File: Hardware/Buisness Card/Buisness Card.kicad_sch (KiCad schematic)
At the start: 24 parts, among them J101 USB_A, J102 Conn_01x03_Male, J103 Tag Connect, U101 NCP1117-12_SOT223, U102 ATtiny85-20S, U103 ProtoBoard

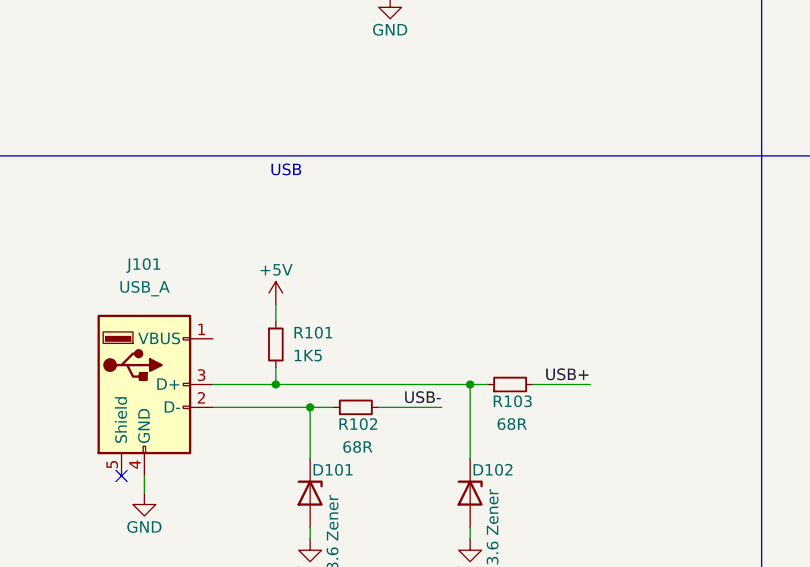
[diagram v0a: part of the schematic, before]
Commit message: put diode in the right way
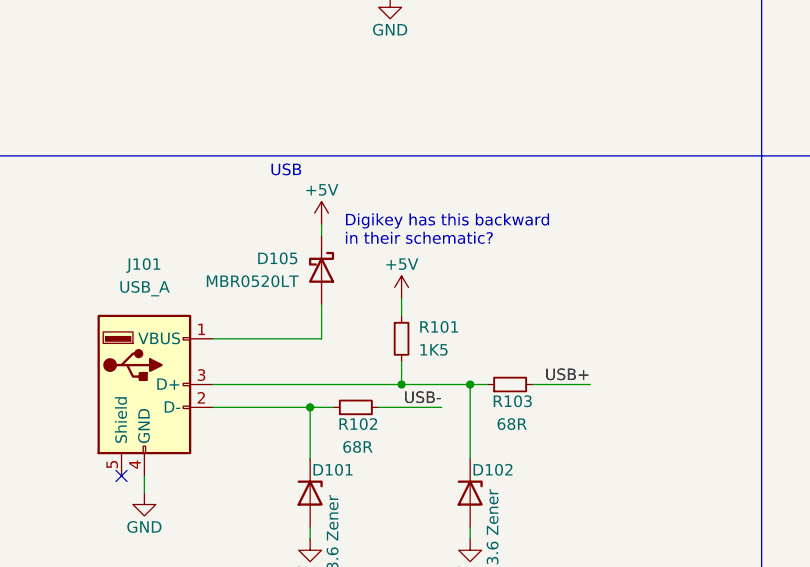
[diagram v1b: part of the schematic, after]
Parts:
- added D105: MBR0520LT, Diode_SMD:D_SOD-123, symbol Diode:MBR0520LT
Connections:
- net +5V: now also D105.1 (K)
- net at J101.1 (VBUS): now also D105.2 (A)
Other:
- note added: "Digikey has this backward in their schematic?"
- moved on the sheet: R101
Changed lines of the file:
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@@
   (junction (at 81.915 35.56) (diameter 0) (color 0 0 0 0)
   )
-  (junction (at 57.15 91.44) (diameter 0) (color 0 0 0 0)
+  (junction (at 71.12 91.44) (diameter 0) (color 0 0 0 0)
   )
   (junction (at 78.74 91.44) (diameter 0) (color 0 0 0 0)
@@
     (stroke (width 0) (type default) (color 0 0 0 0))
   )
-  (wire (pts (xy 57.15 91.44) (xy 57.15 89.535))
-    (stroke (width 0) (type default) (color 0 0 0 0))
-  )
   (wire (pts (xy 137.795 185.42) (xy 150.495 185.42))
     (stroke (width 0) (type default) (color 0 0 0 0))
@@
     (stroke (width 0) (type default) (color 0 0 0 0))
   )
-  (wire (pts (xy 50.165 91.44) (xy 57.15 91.44))
+  (wire (pts (xy 50.165 91.44) (xy 71.12 91.44))
     (stroke (width 0) (type default) (color 0 0 0 0))
   )
@@
     (stroke (width 0) (type default) (color 0 0 0 0))
   )
+  (wire (pts (xy 50.165 86.36) (xy 62.23 86.36))
+    (stroke (width 0) (type default) (color 0 0 0 0))
+  )
   (wire (pts (xy 18.415 182.245) (xy 18.415 180.975))
     (stroke (width 0) (type default) (color 0 0 0 0))
@@
     (stroke (width 0) (type default) (color 0 0 0 0))
   )
+  (wire (pts (xy 62.23 86.36) (xy 62.23 82.55))
+    (stroke (width 0) (type default) (color 0 0 0 0))
+  )
   (wire (pts (xy 85.09 32.385) (xy 85.09 35.56))
     (stroke (width 0) (type default) (color 0 0 0 0))
@@
     (stroke (width 0) (type default) (color 0 0 0 0))
   )
-  (wire (pts (xy 57.15 91.44) (xy 78.74 91.44))
+  (wire (pts (xy 71.12 91.44) (xy 78.74 91.44))
     (stroke (width 0) (type default) (color 0 0 0 0))
   )
@@
     (stroke (width 0) (type default) (color 0 0 0 0))
   )
+  (wire (pts (xy 62.23 73.66) (xy 62.23 74.93))
+    (stroke (width 0) (type default) (color 0 0 0 0))
+  )
   (wire (pts (xy 137.795 182.88) (xy 150.495 182.88))
     (stroke (width 0) (type default) (color 0 0 0 0))
@@
     (stroke (width 0) (type default) (color 0 0 0 0))
   )
+  (wire (pts (xy 71.12 88.9) (xy 71.12 91.44))
+    (stroke (width 0) (type default) (color 0 0 0 0))
+  )
   (wire (pts (xy 243.205 41.91) (xy 243.205 43.18))
     (stroke (width 0) (type default) (color 0 0 0 0))
@@
     (stroke (width 0) (type default) (color 0 0 0 0))
   )
-  (wire (pts (xy 57.15 82.55) (xy 57.15 84.455))
+  (wire (pts (xy 71.12 81.915) (xy 71.12 83.82))
     (stroke (width 0) (type default) (color 0 0 0 0))
   )
@@
   )
   (text "Ask dad if this is ok setup" (at 27.94 33.02 0)
+    (effects (font (size 1.27 1.27)) (justify left bottom))
+  )
+  (text "Digikey has this backward\nin their schematic?" (at 64.77 76.2 0)
     (effects (font (size 1.27 1.27)) (justify left bottom))
   )
@@
     (pin "7")
     (pin "8")
+  )
+  (symbol (lib_id "power:+5V") (at 62.23 73.66 0) (unit 1)
+    (in_bom yes) (on_board yes)
+    (property "Reference" "#PWR?" (id 0) (at 62.23 77.47 0)
+      (effects (font (size 1.27 1.27)) hide)
+    )
+    (property "Value" "+5V" (id 1) (at 62.23 69.85 0))
+    (property "Footprint" "" (id 2) (at 62.23 73.66 0)
+      (effects (font (size 1.27 1.27)) hide)
+    )
+    (property "Datasheet" "" (id 3) (at 62.23 73.66 0)
+      (effects (font (size 1.27 1.27)) hide)
+    )
+    (pin "1")
   )
   (symbol (lib_id "Connector_Generic:Conn_02x05_Odd_Even") (at 158.115 182.88 180) (unit 1)
@@
     (pin "1")
   )
+  (symbol (lib_id "Diode:MBR0520LT") (at 62.23 78.74 270) (unit 1)
+    (in_bom yes) (on_board yes)
+    (property "Reference" "D105" (id 0) (at 59.69 77.47 90)
+      (effects (font (size 1.27 1.27)) (justify right))
+    )
+    (property "Value" "MBR0520LT" (id 1) (at 59.69 80.01 90)
+      (effects (font (size 1.27 1.27)) (justify right))
+    )
+    (property "Footprint" "Diode_SMD:D_SOD-123" (id 2) (at 57.785 78.74 0)
+      (effects (font (size 1.27 1.27)) hide)
+    )
+    (property "Datasheet" "http://www.onsemi.com/pub_link/Collateral/MBR0520LT1-D.PDF" (id 3) (at 62.23 78.74 0)
+      (effects (font (size 1.27 1.27)) hide)
+    )
+    (pin "1")
+    (pin "2")
+  )
   (symbol (lib_id "power:+5V") (at 165.1 175.895 0) (unit 1)
     (in_bom yes) (on_board yes)
@@
     (pin "1")
   )
-  (symbol (lib_id "Device:R_Small") (at 57.15 86.995 0) (unit 1)
-    (in_bom yes) (on_board yes)
-    (property "Reference" "R101" (id 0) (at 59.055 85.725 0)
-      (effects (font (size 1.27 1.27)) (justify left))
-    )
-    (property "Value" "1K5" (id 1) (at 59.055 88.265 0)
-      (effects (font (size 1.27 1.27)) (justify left))
-    )
-    (property "Footprint" "Resistor_SMD:R_0805_2012Metric" (id 2) (at 57.15 86.995 0)
-      (effects (font (size 1.27 1.27)) hide)
-    )
-    (property "Datasheet" "~" (id 3) (at 57.15 86.995 0)
+  (symbol (lib_id "Device:R_Small") (at 71.12 86.36 0) (unit 1)
+    (in_bom yes) (on_board yes)
+    (property "Reference" "R101" (id 0) (at 73.025 85.09 0)
+      (effects (font (size 1.27 1.27)) (justify left))
+    )
+    (property "Value" "1K5" (id 1) (at 73.025 87.63 0)
+      (effects (font (size 1.27 1.27)) (justify left))
+    )
+    (property "Footprint" "Resistor_SMD:R_0805_2012Metric" (id 2) (at 71.12 86.36 0)
+      (effects (font (size 1.27 1.27)) hide)
+    )
+    (property "Datasheet" "~" (id 3) (at 71.12 86.36 0)
       (effects (font (size 1.27 1.27)) hide)
     )
@@
     (pin "1")
   )
-  (symbol (lib_id "power:+5V") (at 57.15 82.55 0) (unit 1)
-    (in_bom yes) (on_board yes)
-    (property "Reference" "#PWR0106" (id 0) (at 57.15 86.36 0)
-      (effects (font (size 1.27 1.27)) hide)
-    )
-    (property "Value" "+5V" (id 1) (at 57.15 78.74 0))
-    (property "Footprint" "" (id 2) (at 57.15 82.55 0)
-      (effects (font (size 1.27 1.27)) hide)
-    )
-    (property "Datasheet" "" (id 3) (at 57.15 82.55 0)
+  (symbol (lib_id "power:+5V") (at 71.12 81.915 0) (unit 1)
+    (in_bom yes) (on_board yes)
+    (property "Reference" "#PWR0106" (id 0) (at 71.12 85.725 0)
+      (effects (font (size 1.27 1.27)) hide)
+    )
+    (property "Value" "+5V" (id 1) (at 71.12 78.105 0))
+    (property "Footprint" "" (id 2) (at 71.12 81.915 0)
+      (effects (font (size 1.27 1.27)) hide)
+    )
+    (property "Datasheet" "" (id 3) (at 71.12 81.915 0)
       (effects (font (size 1.27 1.27)) hide)
     )
@@
       (reference "#PWR0123") (unit 1) (value "GND") (footprint "")
     )
+    (path "/03fe99ca-f25a-4603-971e-459a2c3cea1a"
+      (reference "#PWR?") (unit 1) (value "+5V") (footprint "")
+    )
     (path "/9e3048d5-0d17-4b49-a16b-c4612d611db7"
       (reference "C101") (unit 1) (value "1μf") (footprint "Capacitor_SMD:C_0805_2012Metric")
@@
       (reference "D104") (unit 1) (value "PWR") (footprint "LED_SMD:LED_0805_2012Metric")
     )
+    (path "/52983eb2-ee43-43ac-aa36-588ea223af84"
+      (reference "D105") (unit 1) (value "MBR0520LT") (footprint "Diode_SMD:D_SOD-123")
+    )
     (path "/08fbe3c8-eeef-411e-a21c-af2a017d4a38"

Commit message: Update a few things
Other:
- title: (none) -> Contact Card
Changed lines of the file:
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@@
 (kicad_sch (version 20211123) (generator eeschema)
   (paper "A4")
+  (title_block
+    (title "Contact Card")
+    (date "${ISSUE}")
+    (rev "${REVISION}")
+    (comment 4 "${FULL_REVISION}")
+  )
   (junction (at 81.915 35.56) (diameter 0) (color 0 0 0 0)
   )

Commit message: V2.0 Design (#1)
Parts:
- C103: value 4.7uf -> 5pf
- J103: footprint Connector:Tag-Connect_TC2050-IDC-NL_2x05_P1.27mm_Vertical -> Connector:Tag-Connect_TC2050-IDC-FP_2x05_P1.27mm_Vertical
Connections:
- net USB+: now also D102.1 (K), J101.3 (D+), R101.2, R103.1; no longer JP101.1 (A), R103.2, U102.2 (XTAL1/PB3)
- net USB-: now also D101.1 (K), J101.2 (D-), R102.1; no longer JP102.1 (A), R102.2, U102.3 (XTAL2/PB4)
- new net USBA: JP101.1 (A), R103.2, U102.2 (XTAL1/PB3)
- new net USBB: JP102.1 (A), R102.2, U102.3 (XTAL2/PB4)
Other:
- note removed: "Ask dad if this is ok setup"
- moved on the sheet: C101, J102

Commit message: Fix for #2
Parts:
- C101: LCSC# (none) -> C28323
- C102, C104: LCSC# (none) -> C138340
- C103: LCSC# (none) -> C1824
- D101, D102: LCSC# (none) -> C2891771
- D103, D104: LCSC# (none) -> C84256
- D105: LCSC# (none) -> C165467
- R101: LCSC# (none) -> C325846
- R102, R103: LCSC# (none) -> C17802
- R104, R105: LCSC# (none) -> C17513
- U102: LCSC# (none) -> C89852
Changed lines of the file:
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@@
+      (effects (font (size 1.27 1.27)) hide)
+    )
+    (property "LCSC#" "C17802" (at 66.04 93.98 90)
       (effects (font (size 1.27 1.27)) hide)
     )
@@
       (effects (font (size 1.27 1.27)) hide)
     )
+    (property "LCSC#" "C165467" (at 62.23 78.74 90)
+      (effects (font (size 1.27 1.27)) hide)
+    )
     (pin "1")
     (pin "2")
@@
     )
     (property "Datasheet" "~" (at 71.12 86.36 0)
+      (effects (font (size 1.27 1.27)) hide)
+    )
+    (property "LCSC#" "C325846" (at 71.12 86.36 0)
       (effects (font (size 1.27 1.27)) hide)
     )
@@
       (effects (font (size 1.27 1.27)) hide)
     )
+    (property "LCSC#" "C84256" (at 243.205 38.1 0)
+      (effects (font (size 1.27 1.27)) hide)
+    )
     (pin "1")
     (pin "2")
@@
   (symbol (lib_id "Device:R_Small") (at 243.205 45.72 180) (unit 1)
     (in_bom yes) (on_board yes) (dnp no)
-    (property "Reference" "R104" (at 248.92 45.085 0)
-      (effects (font (size 1.27 1.27)) (justify left))
-    )
-    (property "Value" "1K" (at 247.015 46.99 0)
-      (effects (font (size 1.27 1.27)) (justify left))
+    (property "Reference" "R104" (at 244.475 45.085 0)
+      (effects (font (size 1.27 1.27)) (justify right))
+    )
+    (property "Value" "1K" (at 244.475 46.99 0)
+      (effects (font (size 1.27 1.27)) (justify right))
     )
     (property "Footprint" "Resistor_SMD:R_0805_2012Metric" (at 243.205 45.72 0)
@@
     )
     (property "Datasheet" "~" (at 243.205 45.72 0)
+      (effects (font (size 1.27 1.27)) hide)
+    )
+    (property "LCSC#" "C17513" (at 243.205 45.72 0)
       (effects (font (size 1.27 1.27)) hide)
     )
@@
       (effects (font (size 1.27 1.27)) hide)
     )
+    (property "LCSC#" "C84256" (at 253.365 38.1 0)
+      (effects (font (size 1.27 1.27)) hide)
+    )
     (pin "1")
     (pin "2")
@@
       (effects (font (size 1.27 1.27)) hide)
     )
+    (property "LCSC#" "C2891771" (at 60.96 103.505 90)
+      (effects (font (size 1.27 1.27)) hide)
+    )
     (pin "1")
     (pin "2")
@@
     )
     (property "Datasheet" "http://ww1.microchip.com/downloads/en/DeviceDoc/atmel-2586-avr-8-bit-microcontroller-attiny25-attiny45-attiny85_datasheet.pdf" (at 136.525 102.235 0)
+      (effects (font (size 1.27 1.27)) hide)
+    )
+    (property "LCSC#" "C89852" (at 136.525 102.235 0)
       (effects (font (size 1.27 1.27)) hide)
     )
@@
       (effects (font (size 1.27 1.27)) hide)
     )
+    (property "LCSC#" "C138340" (at 153.035 76.835 0)
+      (effects (font (size 1.27 1.27)) hide)
+    )
     (pin "1")
     (pin "2")
@@
       (effects (font (size 1.27 1.27)) hide)
     )
+    (property "LCSC#" "C138340" (at 81.915 41.275 0)
+      (effects (font (size 1.27 1.27)) hide)
+    )
     (pin "1")
     (pin "2")
@@
       (effects (font (size 1.27 1.27)) hide)
     )
+    (property "LCSC#" "C28323" (at 56.515 40.64 0)
+      (effects (font (size 1.27 1.27)) hide)
+    )
     (pin "1")
     (pin "2")
@@
   (symbol (lib_id "Device:R_Small") (at 253.365 45.72 180) (unit 1)
     (in_bom yes) (on_board yes) (dnp no)
-    (property "Reference" "R105" (at 259.08 44.45 0)
-      (effects (font (size 1.27 1.27)) (justify left))
-    )
-    (property "Value" "1K" (at 257.175 46.99 0)
-      (effects (font (size 1.27 1.27)) (justify left))
+    (property "Reference" "R105" (at 255.27 44.45 0)
+      (effects (font (size 1.27 1.27)) (justify right))
+    )
+    (property "Value" "1K" (at 255.27 46.99 0)
+      (effects (font (size 1.27 1.27)) (justify right))
     )
     (property "Footprint" "Resistor_SMD:R_0805_2012Metric" (at 253.365 45.72 0)
@@
     )
     (property "Datasheet" "~" (at 253.365 45.72 0)
+      (effects (font (size 1.27 1.27)) hide)
+    )
+    (property "LCSC#" "C17513" (at 253.365 45.72 0)
       (effects (font (size 1.27 1.27)) hide)
     )
@@
       (effects (font (size 1.27 1.27)) hide)
     )
+    (property "LCSC#" "C2891771" (at 78.74 103.505 90)
+      (effects (font (size 1.27 1.27)) hide)
+    )
     (pin "1")
     (pin "2")
@@
     )
     (property "Datasheet" "~" (at 83.185 91.44 0)
+      (effects (font (size 1.27 1.27)) hide)
+    )
+    (property "LCSC#" "C17802" (at 83.185 91.44 90)
       (effects (font (size 1.27 1.27)) hide)
     )
@@
       (effects (font (size 1.27 1.27)) hide)
     )
+    (property "LCSC#" "C1824" (at 142.875 76.835 0)
+      (effects (font (size 1.27 1.27)) hide)
+    )
